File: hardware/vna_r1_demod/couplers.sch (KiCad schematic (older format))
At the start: 14 parts, among them U501 CONN_SMA_2GND, U502 resistive_bridge, U503 resistive_bridge, U504 CONN_SMA_2GND

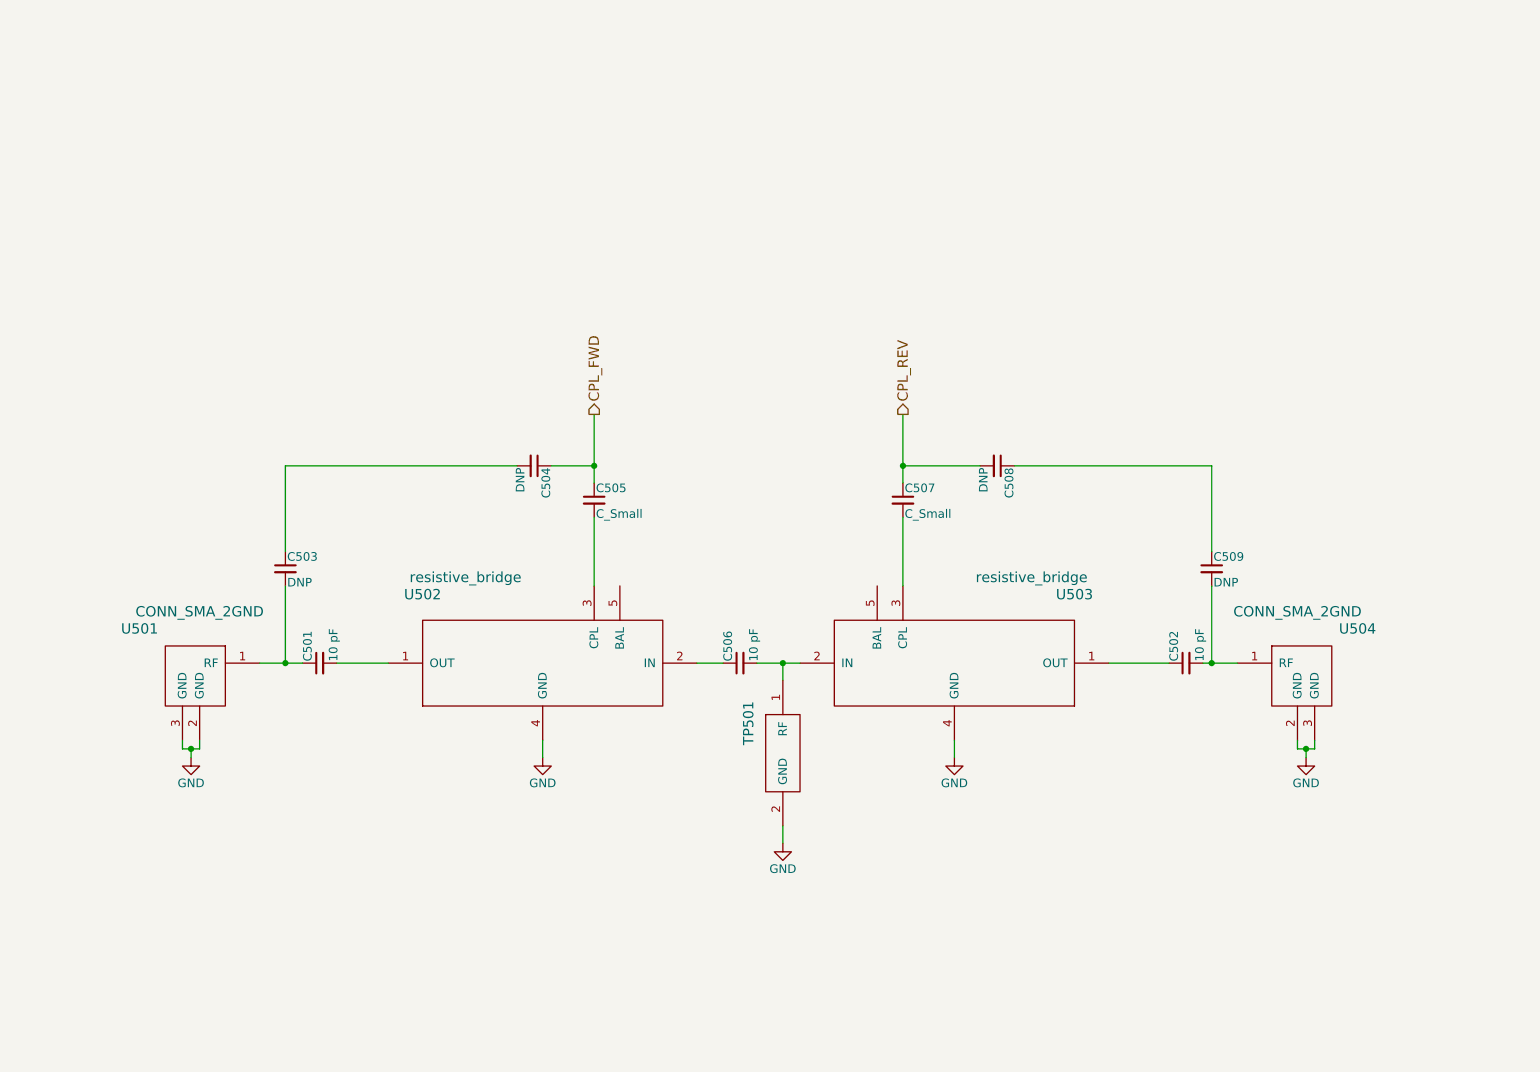
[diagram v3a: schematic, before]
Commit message: work on demod - added fixed attenuator to ref path, fixed bridge symbol and footprint
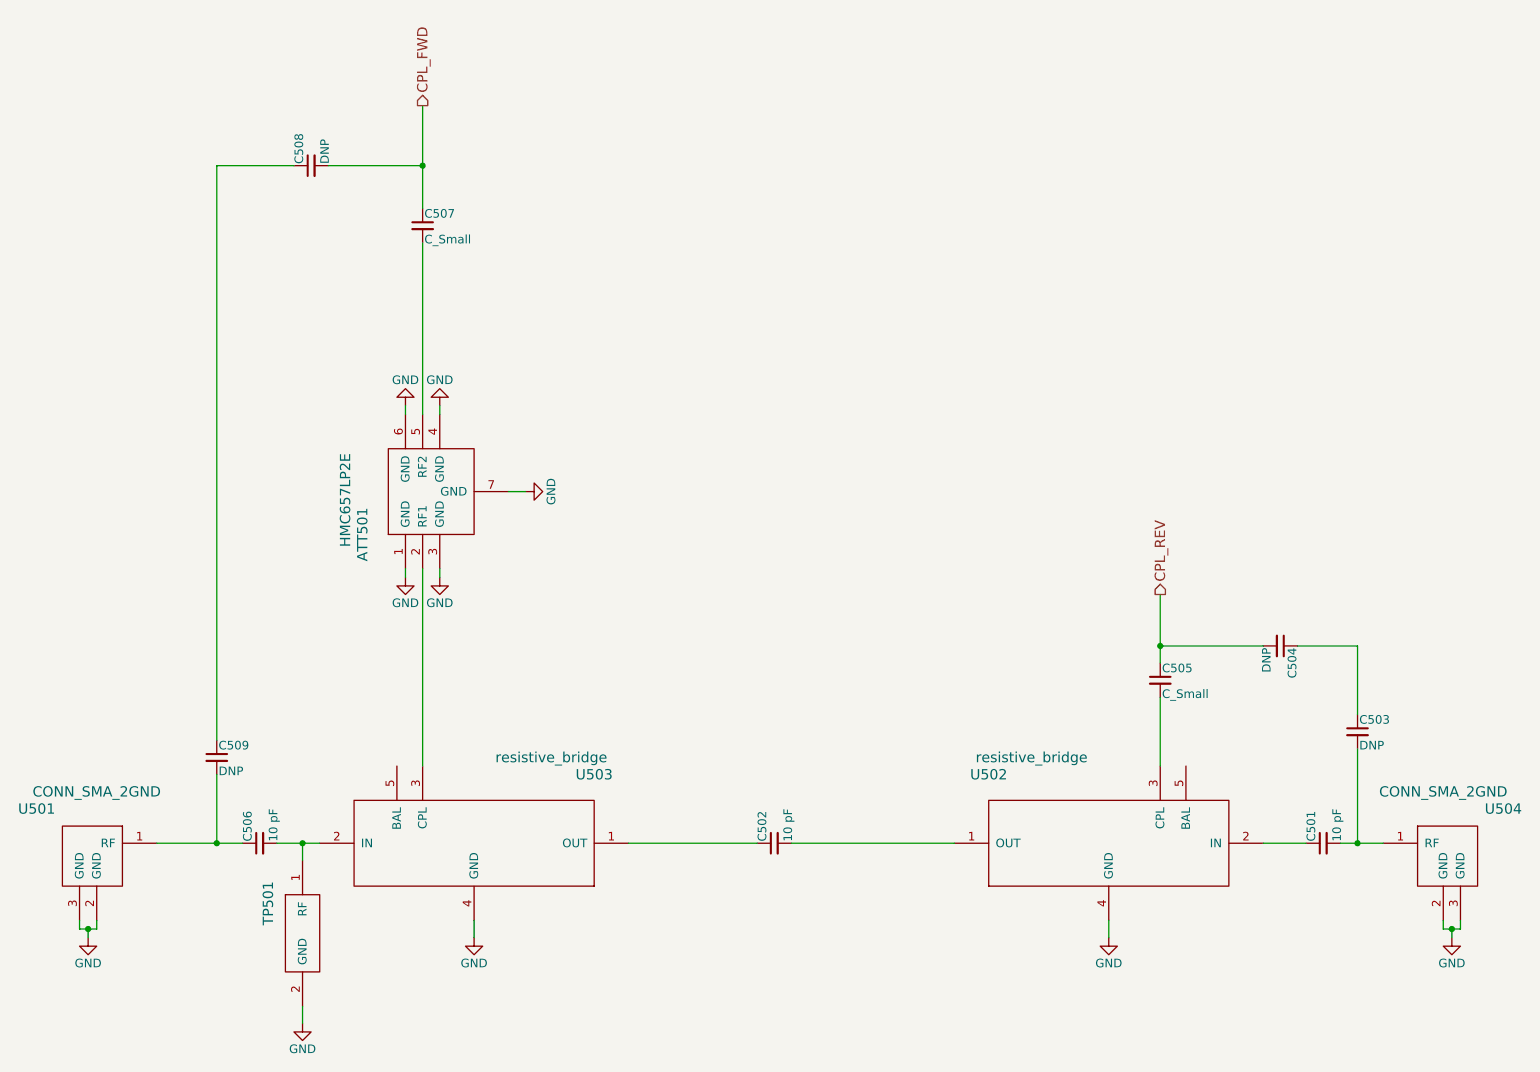
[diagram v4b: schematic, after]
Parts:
- added ATT501: HMC657LP2E, Housings_DFN_QFN:DFN-6-1EP_2x2mm_Pitch0.65mm, symbol HMC65XLP2E
- U502: footprint vna_footprints:resistive_bridge_osh_fr408_ustrip -> vna_footprints:resistive_bridge_osh_fr408_ustrip_mirrored
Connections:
- net CPL_FWD: now also C507.1, C508.2; no longer C504.1, C505.1
- net CPL_REV: now also C504.2, C505.1; no longer C507.1, C508.2
- net GND: now also ATT501.1 (GND), ATT501.3 (GND), ATT501.4 (GND), ATT501.6 (GND), ATT501.7 (GND)
- net at U502.1 (OUT): now also C502.2; no longer C501.2
- net at U502.2 (IN): now also C501.1; no longer C506.1
- net at U503.3 (CPL): now also ATT501.2 (RF1); no longer C507.2
- net at C503.1: now also C504.1; no longer C504.2
- new net: C506.1, C509.2, U501.1 (RF)
- new net: C501.2, C503.2, U504.1 (RF)
- new net: ATT501.5 (RF2), C507.2
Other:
- moved on the sheet: C502, C503, C504, C505, C506, C507, C508, C509, TP501, U501, U502, U503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
